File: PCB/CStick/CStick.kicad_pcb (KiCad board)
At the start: 2 copper layers, 39.1 x 31.5 mm, 7 parts, among them J1 Conn_01x04_Male, U1 Stickbox_Assembly

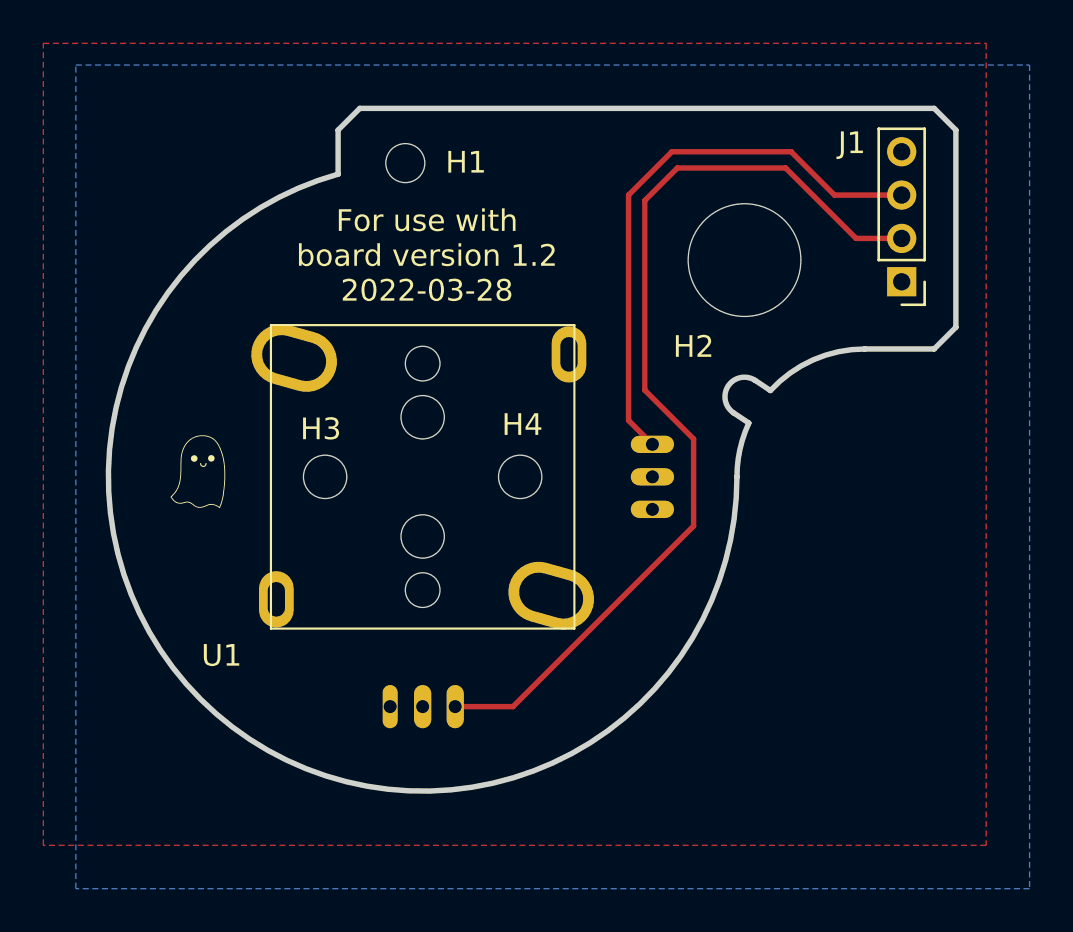
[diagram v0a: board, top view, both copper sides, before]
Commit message: applied footprint changes to all pcbs
forgot to change cstick and motherboard to reflect the new hall sensor footprint, fixed now.
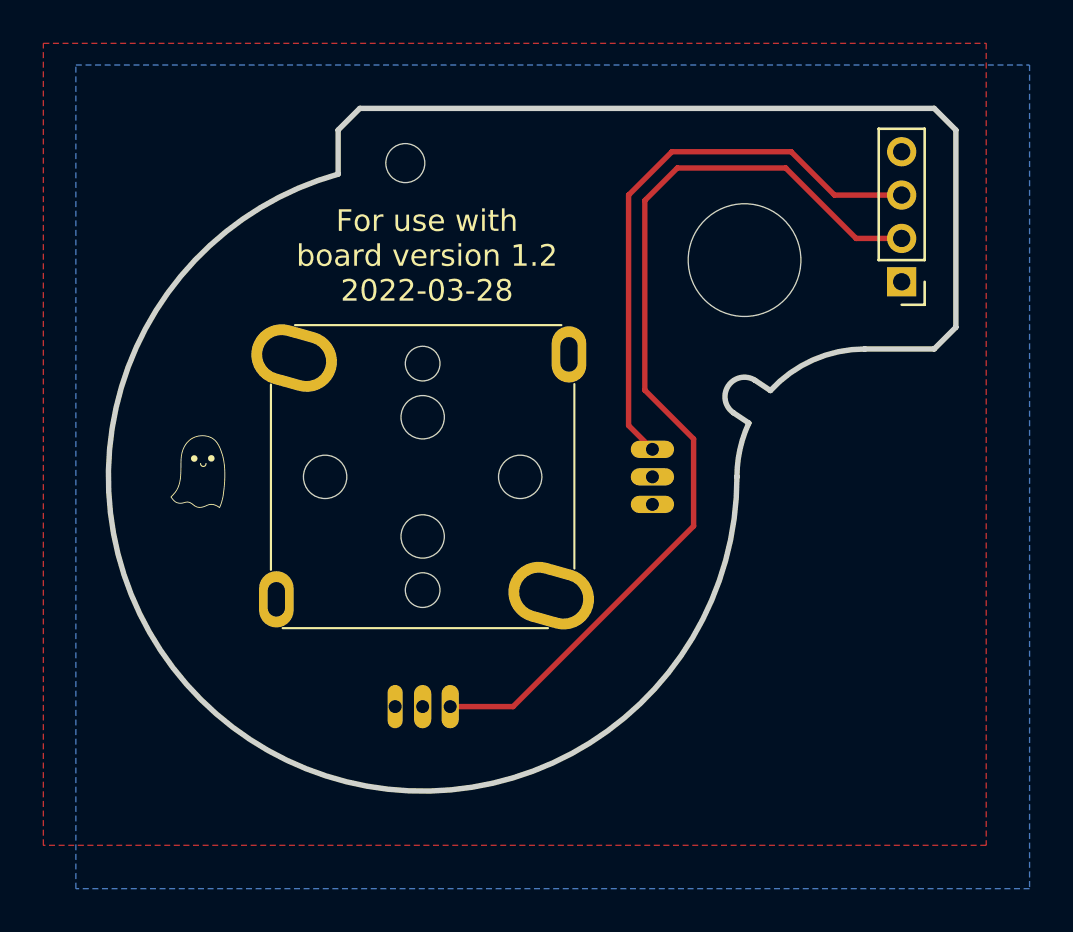
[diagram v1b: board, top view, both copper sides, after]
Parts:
- H1: footprint Gamecube MB:MountingHole_1.8mm -> PhobGCC_Footprints:MountingHole_1.8mm
- H2: footprint Gamecube MB:MountingHole_5.2mm -> PhobGCC_Footprints:MountingHole_5.2mm
- H3, H4: footprint Gamecube MB:MountingHole_2.0mm -> PhobGCC_Footprints:MountingHole_2.0mm
- U1: footprint Gamecube MB:GCC_Stickbox_Hall_Only -> PhobGCC_Footprints:GCC_Stickbox_Hall_Only
